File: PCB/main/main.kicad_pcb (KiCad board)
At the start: 2 copper layers, 98.7 x 98.7 mm, 50 parts, among them IC1 LM358DR2G, IC2 ap2007, IC3 TP4056-42-ESOP8, IC4 LM3940IMP-3.3_NOPB, IC5 CP2102-GMR, J1 Conn_01x33_Female, J2 Conn_01x33_Female, J3 Conn_01x33_Female, J4 Conn_01x33_Female, Q1 AO3401A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

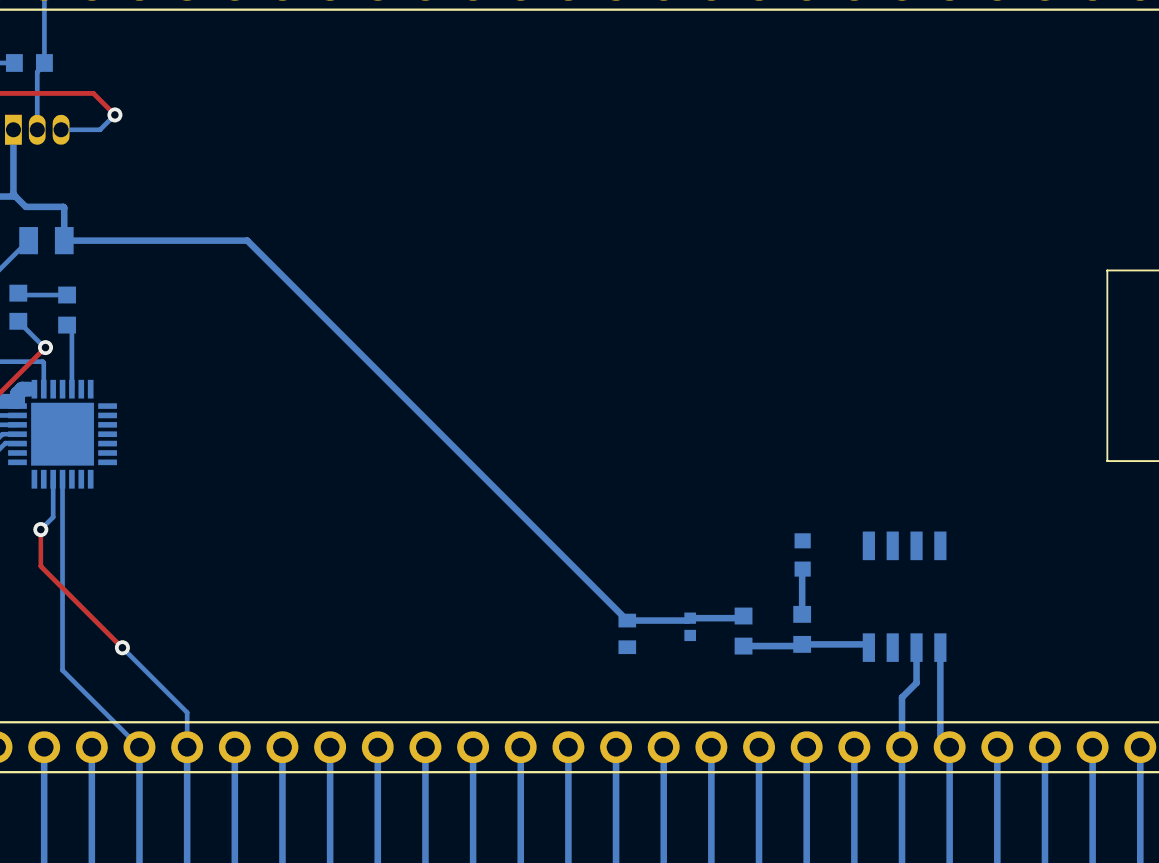
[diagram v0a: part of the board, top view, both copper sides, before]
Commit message: Updated MC Interfacing with pullups
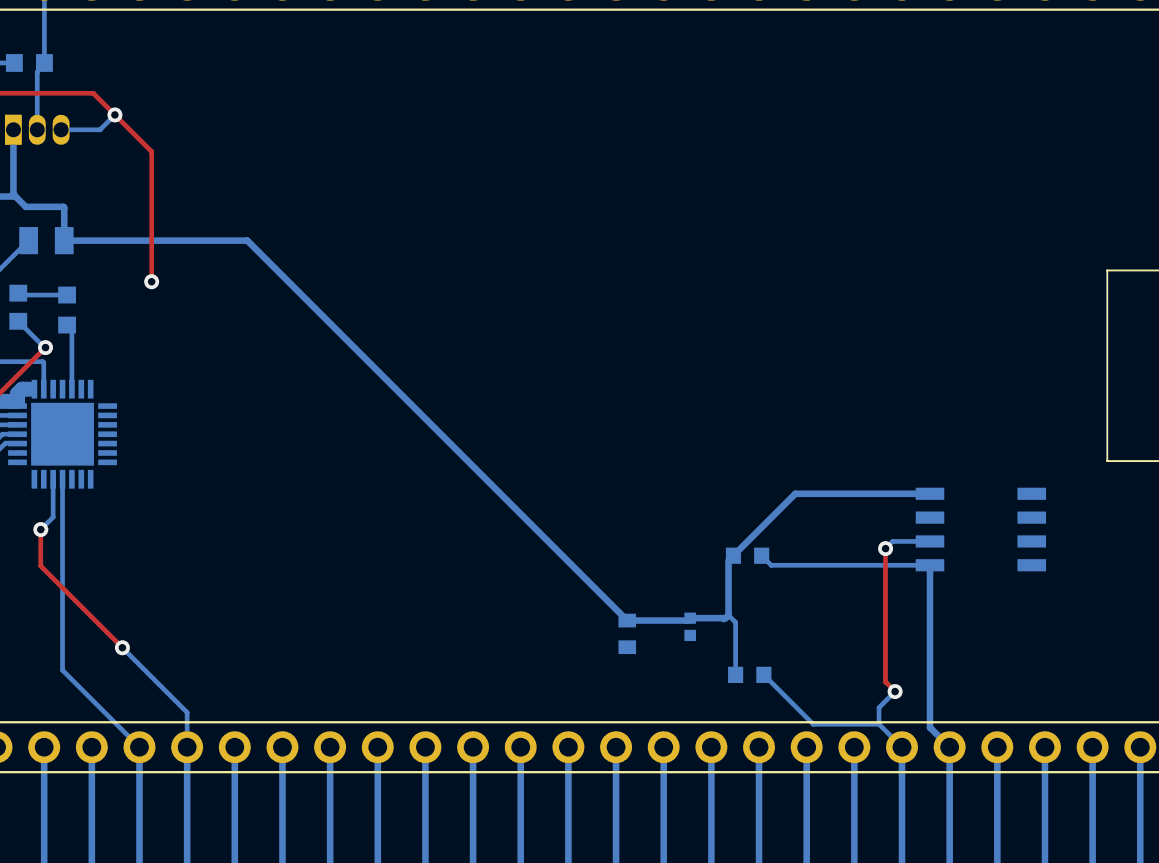
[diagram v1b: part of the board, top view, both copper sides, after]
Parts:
- removed R10: 120R, EEE3088F_Footprints:R0603
- removed R8, R9: 1K8, EEE3088F_Footprints:RESC1608X55N
- added R14: 10k, EEE3088F_Footprints:R0603, B.Cu at (159.3, 106.0)
- added R15: 10k, EEE3088F_Footprints:R0603, B.Cu at (159.4, 112.4)
- moved U3 5.42 mm to (171.7, 104.6), turned to 180 degrees
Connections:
- U3 pad 8: /1V7 -> /3V3
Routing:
- net /3V3: track 124.1 -> 142.1 mm
- net /PB6: track 15.8 -> 31.6 mm, vias 0 -> 2
- net /PB7: track 15.7 -> 29.5 mm
- net GND: track 124.4 -> 134.1 mm, vias 16 -> 17
- net /1V7: track 6.79 -> 0.00 mm
- net Net-(R10-Pad1): track 2.42 -> 0.00 mm

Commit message: Updated footprints
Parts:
- added IC1: MCP6002T-I_SN, EEE3088F_Footprints:SOIC127P600X175-8N, F.Cu at (220.0, 62.2)
- added U1: LM61BIZ/NOPB_TempSensor(TO-92), EEE3088F_Footprints:TO-92-3_L4.9-W3.7-P1.27-L, F.Cu at (216.2, 75.9)
- added U2: LPS22HBTR_Barometer, EEE3088F_Footprints:QFN50P210X200X80-10N, F.Cu at (221.4, 75.0)
- U4: footprint EEE3088F_Footprints(new):MICRO-USB-SMD_MICROXNJ -> EEE3088F_Footprints:MICRO-USB-SMD_MICROXNJ
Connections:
- BT1 pad 2: /Power/BAT- -> GND
- IC2 pad 9: unconnected-(IC2-Pad9) -> GND
- IC3 pad 1: /Power/BAT- -> GND
- IC3 pad 9: unconnected-(IC3-Pad9) -> GND
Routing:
- net GND: track 134.1 -> 138.6 mm
- net /Power/BAT-: track 4.51 -> 0.00 mm

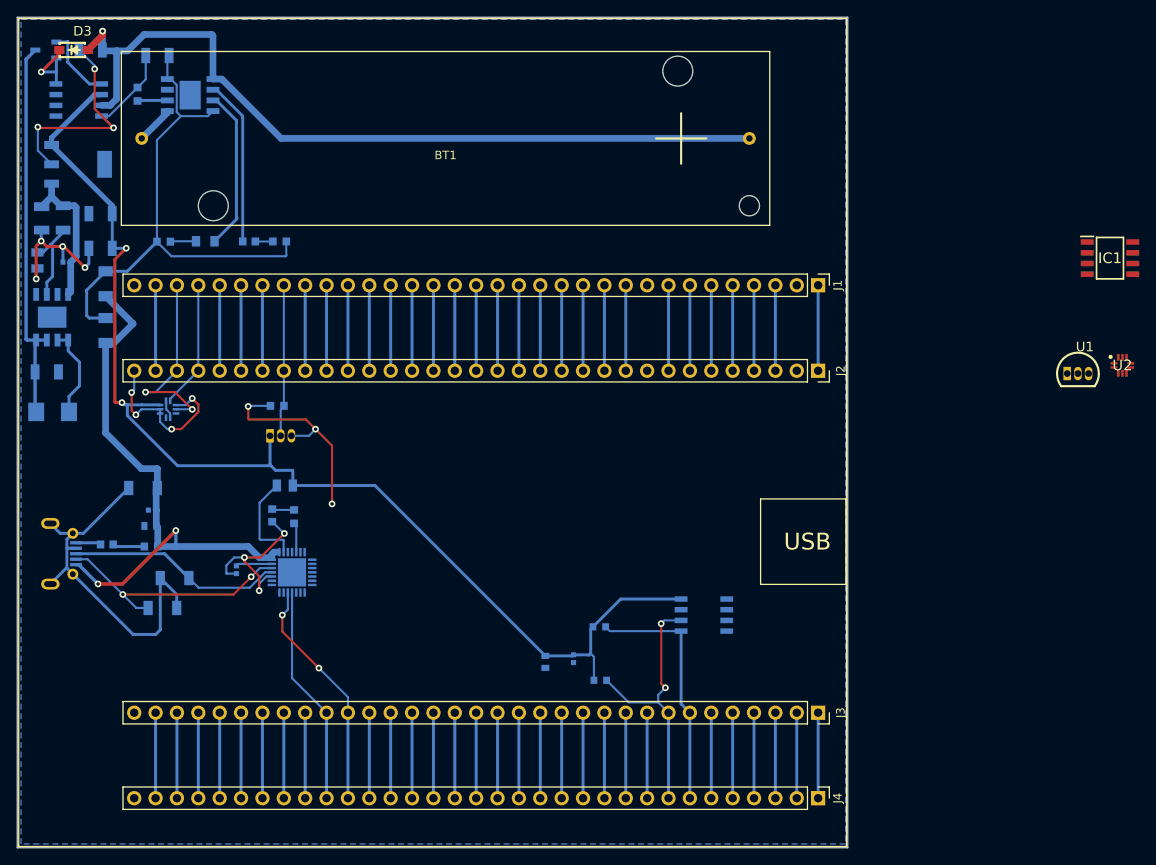
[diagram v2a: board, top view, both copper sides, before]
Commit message: Fixed a lot of shit. Added 3 test pads. Rounded PCB corners
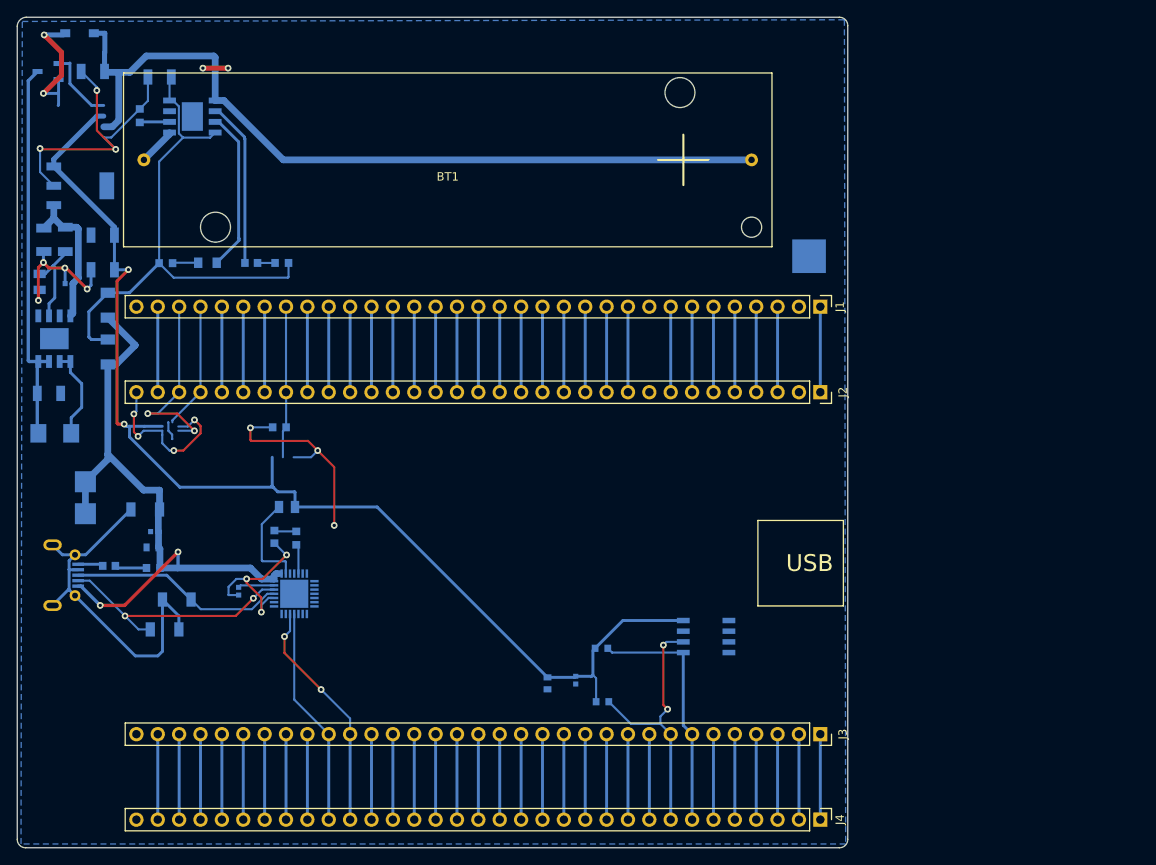
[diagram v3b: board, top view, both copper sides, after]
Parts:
- removed IC1: MCP6002T-I_SN, EEE3088F_Footprints:SOIC127P600X175-8N
- removed IC1: LM358DR2G, EEE3088F_Footprints:SOIC127P600X175-8N
- removed U1: LM61BIZ/NOPB_TempSensor(TO-92), EEE3088F_Footprints:TO-92-3_L4.9-W3.7-P1.27-L
- removed U1: LM61BIZ/NOPD_TempSensor(TO-92), EEE3088F_Footprints:TO-92-3_L4.9-W3.7-P1.27-L
- removed U2 (x2): LPS22HBTR_Barometer, EEE3088F_Footprints:QFN50P210X200X80-10N
- added TP1: 5V Test, TestPoint:TestPoint_Pad_2.5x2.5mm, B.Cu at (98.2, 88.8)
- added TP10: GND TEST, TestPoint:TestPoint_Pad_4.0x4.0mm, B.Cu at (184.2, 62.0)
- added TP7: USB Det, TestPoint:TestPoint_Pad_2.5x2.5mm, B.Cu at (98.2, 92.6)
- D3: moved to B.Cu
- moved R4 2.56 mm to (100.9, 73.4)
- moved C13 2.56 mm to (106.4, 94.7)
- moved J4 2.56 mm to (185.5, 129.0)
- moved C7 2.56 mm to (100.3, 63.6)
- moved D2 2.56 mm to (112.7, 62.8)
- moved C2 2.56 mm to (107.0, 40.7)
- moved R15 2.56 mm to (159.6, 114.9)
- moved C1 2.56 mm to (93.9, 78.3)
- moved C3 2.56 mm to (93.3, 60.0)
- moved C4 2.56 mm to (99.1, 40.0)
- moved C5 2.56 mm to (96.2, 65.2)
- moved C8 2.56 mm to (100.3, 59.5)
- moved C9 2.56 mm to (121.3, 82.3)
- moved D1 2.56 mm to (117.9, 62.8)
- moved D4 2.56 mm to (105.3, 92.1)
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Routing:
- net /USB_5V: track 69.5 -> 77.6 mm
- net Net-(D3-Pad1): track 8.40 -> 16.2 mm, vias 1 -> 2
- net GND: track 138.6 -> 141.6 mm, vias 17 -> 19
- net /Sensing/COMM: track 2.21 -> 0.00 mm
- net (no net): track 0.00 -> 2.21 mm
- net /Power/BAT+: track 98.9 -> 99.5 mm, vias 1 -> 0
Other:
- outline, holes or cut-outs redrawn
- board text added: "+"
- board text added: "5V"
- board text added: "GND"
- board text added: "Positive terminal"

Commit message: Updated PCB with testpads
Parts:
- added IC1: MCP6002T-I_SN, EEE3088F_Footprints:SOIC127P600X175-8N, B.Cu at (97.8, 46.0)
- added TP11: USB_D+, TestPoint:TestPoint_Pad_2.5x2.5mm, B.Cu at (118.0, 107.7)
- added TP12: USB_D-, TestPoint:TestPoint_Pad_2.5x2.5mm, B.Cu at (112.8, 107.8)
- added TP13: 3V3, TestPoint:TestPoint_Pad_2.5x2.5mm, B.Cu at (162.1, 101.0)
- added TP2: Analog Data Read, TestPoint:TestPoint_Pad_2.5x2.5mm, B.Cu at (132.3, 82.4)
- added TP3: MEM_I2C_SDA, TestPoint:TestPoint_Pad_2.5x2.5mm, B.Cu at (175.3, 113.7)
- added TP4: MEM_I2C_SCL, TestPoint:TestPoint_Pad_2.5x2.5mm, B.Cu at (163.3, 112.4)
- added TP5: BARO_I2C_SDA, TestPoint:TestPoint_Pad_2.5x2.5mm, B.Cu at (127.5, 64.0)
- added TP6: BARO_I2C_SCL, TestPoint:TestPoint_Pad_2.5x2.5mm, B.Cu at (115.3, 85.2)
- added TP8: USART_TX, TestPoint:TestPoint_Pad_2.5x2.5mm, B.Cu at (132.6, 114.4)
- added TP9: USART_RX, TestPoint:TestPoint_Pad_2.5x2.5mm, B.Cu at (120.1, 114.4)
- added U1: LM61BIZ/NOPB_TempSensor(TO-92), EEE3088F_Footprints:TO-92-3_L4.9-W3.7-P1.27-L, B.Cu at (121.7, 85.9)
- added U2: LPS22HBTR_Barometer, EEE3088F_Footprints:QFN50P210X200X80-10N, B.Cu at (109.0, 82.5)
- TP10: footprint TestPoint:TestPoint_Pad_4.0x4.0mm -> TestPoint:TestPoint_Pad_2.5x2.5mm
- moved TP7 3.96 mm to (98.0, 88.6)
- moved TP1 3.66 mm to (98.0, 92.5)
- moved TP10 0.06 mm to (184.2, 62.0), turned to 180 degrees
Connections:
- net /microcontroller_interfacing/D+ renamed /USB_D+
- net /microcontroller_interfacing/D- renamed /USB_D-
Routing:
- net GND: track 141.6 -> 124.5 mm, vias 19 -> 17
- net /PB11: track 23.3 -> 36.5 mm, vias 2 -> 1
- net /PC5: track 18.1 -> 28.2 mm
- net /PB10: track 15.1 -> 23.1 mm
- net /PB7: track 29.5 -> 36.5 mm
- net /USB_D-: track 30.0 -> 34.5 mm, vias 2 -> 3
- net /3V3: track 142.1 -> 146.6 mm
- net /PA10: track 27.9 -> 31.9 mm
- net /PB6: track 31.6 -> 35.4 mm
- net /USB_D+: track 25.7 -> 29.5 mm
- net /PA9: track 26.1 -> 29.1 mm
- net (no net): track 2.21 -> 0.00 mm
- net /Sensing/COMM: track 0.00 -> 2.14 mm
- net /5V: track 17.8 -> 17.1 mm
- net Net-(C2-Pad1): track 62.3 -> 61.6 mm
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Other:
- board text added: "3V3"
- board text added: "D+"
- board text added: "D-"
- board text added: "PA10"
- board text added: "PA9"
- board text added: "PB10"
- board text added: "PB11"
- board text added: "PB6"
- board text added: "PB7"
- board text added: "PC5"
- board text added: "USB_5V"
- board text removed: "5V"

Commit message: Finished Gerbers and updated BOM
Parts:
- added G***: LOGO, EEE3088F_Footprints:QRLib, B.Cu at (161.5, 95.5)
- C1, C3, C8: value 22u -> 22uF
- C10: value 100nF -> 0.1uF
- C2, C4, C7: value 10u -> 10uF
- C5: value 0.47u -> 0.47uF
- C6: value 1u -> 1.0uF
- C9: value 1uF -> 1.0uF
- Q1: value AO3401A -> LBSS84LT1G; footprint EEE3088F_Footprints:SOT95P280X125-3N -> EEE3088F_Footprints:SOT96P237X111-3N
- R12: value 4.7k -> 4k7; footprint EEE3088F_Footprints:RESC2013X65N -> EEE3088F_Footprints:RESC1608X55N
- R6: footprint EEE3088F_Footprints:RESC2013X65N -> EEE3088F_Footprints:R0603
- moved U3 31.7 mm to (141.7, 97.5)
- moved R15 26.7 mm to (134.4, 106.3)
- moved TP13 26.6 mm to (139.1, 87.5)
- moved C10 26.2 mm to (138.6, 93.2), turned to 180 degrees
- moved R14 25.6 mm to (134.4, 103.9)
- moved C6 23.2 mm to (141.9, 92.5), turned to 90 degrees
- moved TP4 4.45 mm to (159.8, 115.1)
- moved TP3 3.34 mm to (172.0, 114.2)
- moved Q1 1.44 mm to (93.7, 38.6)
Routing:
- net /3V3: track 146.6 -> 118.2 mm
- net /PB7: track 36.5 -> 63.3 mm
- net /PB6: track 35.4 -> 61.6 mm
- net GND: track 124.5 -> 108.1 mm, vias 17 -> 16
- net Net-(D3-Pad1): track 15.9 -> 18.0 mm
- net /Power/V_UVLO: track 45.6 -> 47.1 mm
- net Net-(IC1-Pad1): track 8.91 -> 9.59 mm
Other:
- board text removed: "USB_5V"

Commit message: Updated Gerbers and DNPs
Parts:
- J1, J4: value Conn_01x33_Female -> Conn_01x33_Male
